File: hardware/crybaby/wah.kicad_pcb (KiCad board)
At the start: 4 copper layers, 99.1 x 87 mm, 39 parts, among them J1 Barrel_Jack_Switch, J2 In, J3 Out, J4 Conn_01x08_Pin, J5 Conn_01x08_Pin, SW2 SW_DIP_x04, SW3 SW_Push_3PDT, U1 TL072, U2 L78L05_TO92

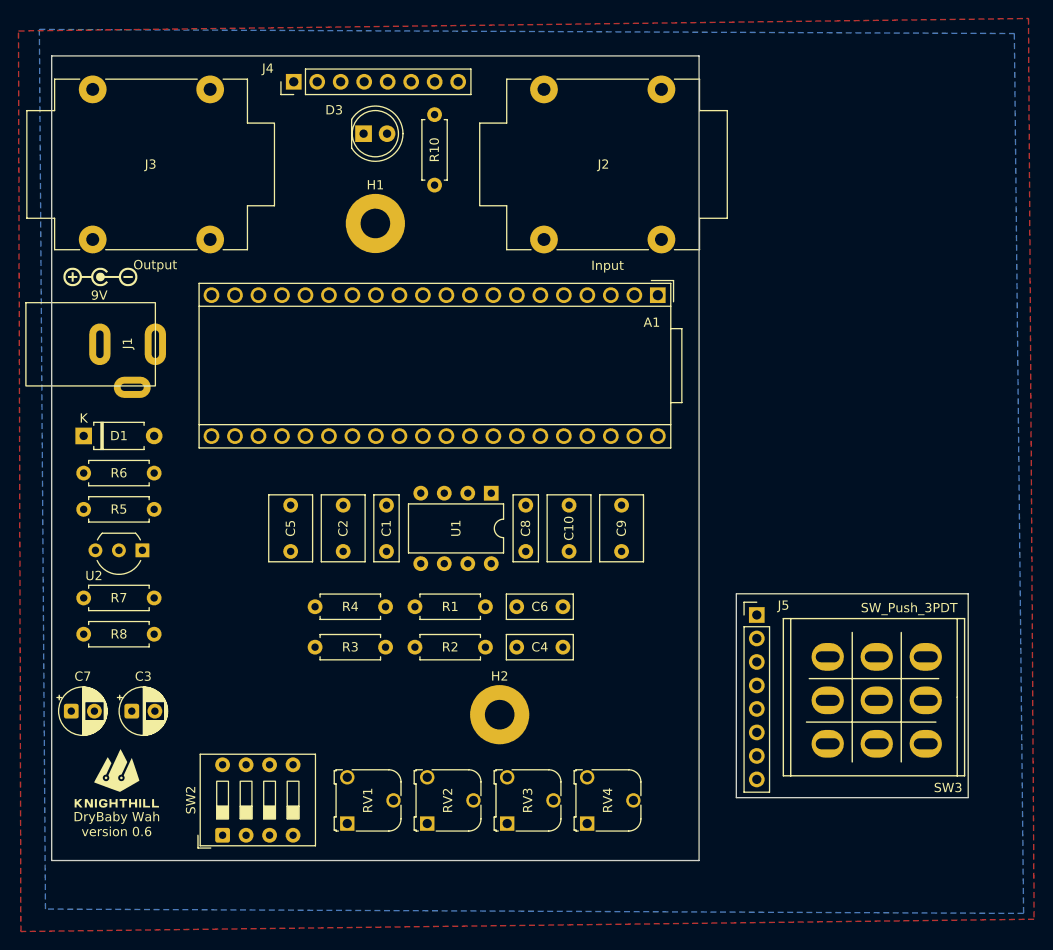
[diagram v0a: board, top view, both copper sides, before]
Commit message: major rearrangement
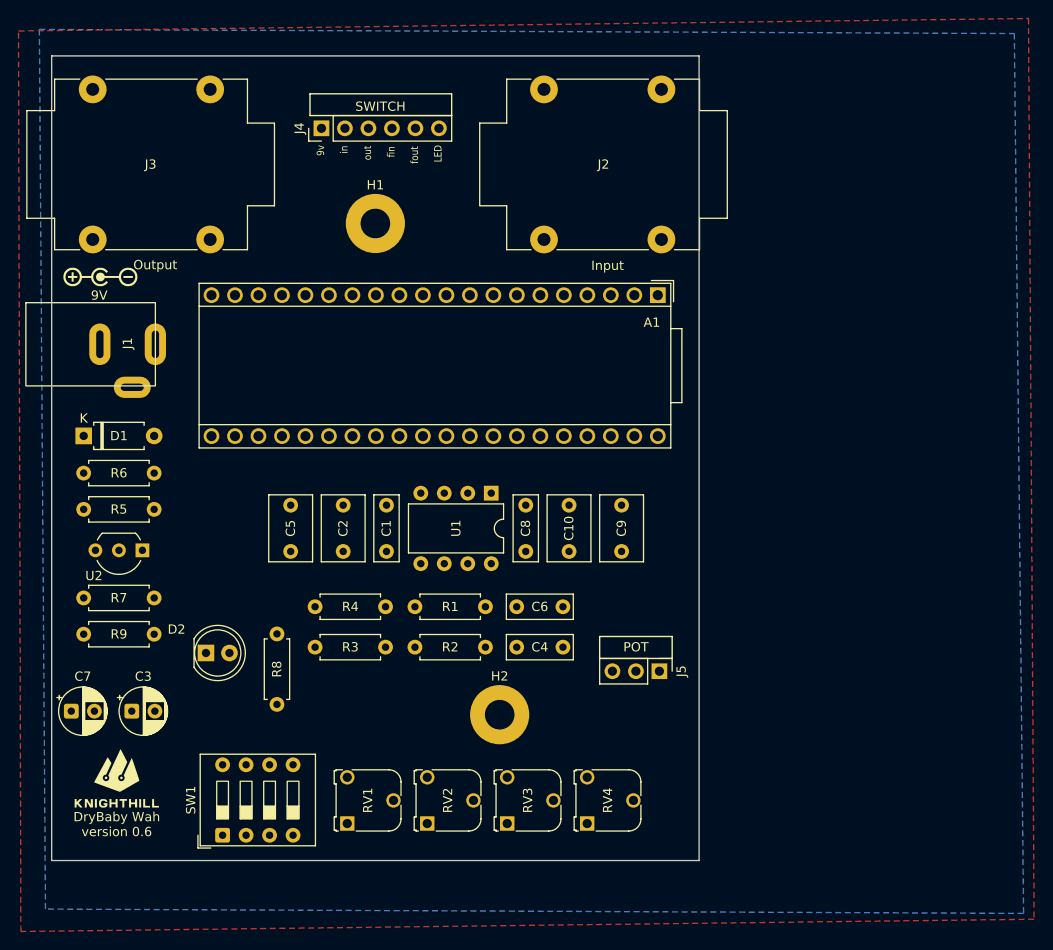
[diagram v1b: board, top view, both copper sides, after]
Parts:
- removed SW3: SW_Push_3PDT, CustomFootprints:Switches_Stomp_Switch_3PDT
- J4: value Conn_01x08_Pin -> Conn_01x06_Pin; footprint Connector_PinHeader_2.54mm:PinHeader_1x08_P2.54mm_Vertical -> Connector_PinHeader_2.54mm:PinHeader_1x06_P2.54mm_Vertical
- J5: value Conn_01x08_Pin -> Conn_01x03_Pin; footprint Connector_PinHeader_2.54mm:PinHeader_1x08_P2.54mm_Vertical -> Connector_PinHeader_2.54mm:PinHeader_1x03_P2.54mm_Vertical
- moved D2 58.7 mm to (59.2, 97.7)
- moved R8 58.7 mm to (66.8, 95.7)
- moved J5 12.2 mm to (108.2, 99.7), turned to -90 degrees
- moved J4 5.86 mm to (71.6, 41.0)
- renumbered D3 to D2, R10 to R8, R8 to R9, SW2 to SW1
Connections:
- A1 pad 26: unconnected-(A1-ADC_4-Pad26) -> /WAH_POT
- J4 pad 1: GND -> +9V
- J4 pad 2: +9V -> /J_IN
- J4 pad 3: /J_IN -> /J_OUT
- J4 pad 4: /J_OUT -> /FX_IN
- J4 pad 5: /FX_IN -> /FX_OUT
- J4 pad 6: /FX_OUT -> /LED
- J5 pad 2: Net-(J5-Pin_2) -> /WAH_POT
- J5 pad 3: Net-(J5-Pin_3) -> VDD
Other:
- board size 99.1 x 87 mm -> 70 x 87 mm
- board text added: "9v"
- board text added: "LED"
- board text added: "POT"
- board text added: "SWITCH"
- board text added: "fin"
- board text added: "fout"
- board text added: "in"
- board text added: "out"

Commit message: fix mirror
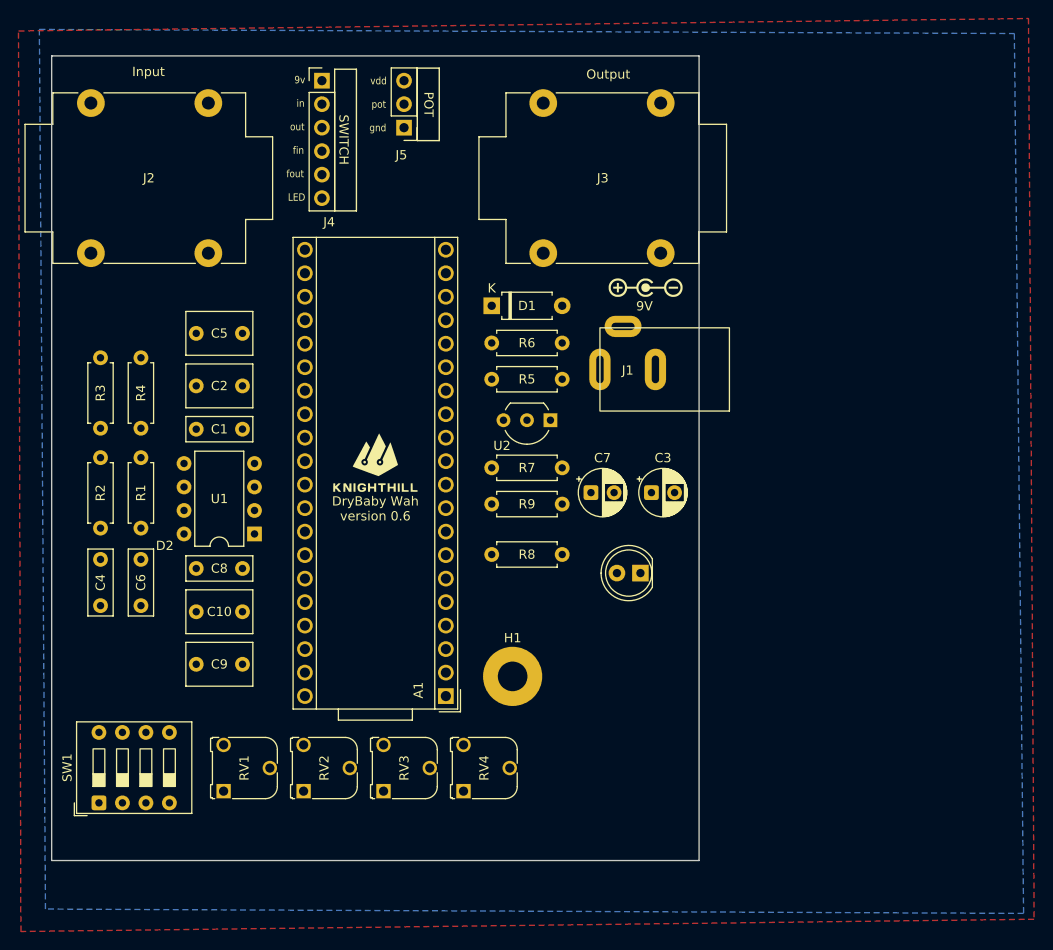
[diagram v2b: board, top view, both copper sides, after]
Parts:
- removed H2: MountingHole_Pad, MountingHole:MountingHole_3.2mm_M3_Pad
- moved J5 64.9 mm to (80.6, 40.9), turned to 180 degrees
- moved C7 61.0 mm to (100.8, 80.4)
- moved C3 61.0 mm to (107.3, 80.4)
- moved G*** 59.0 mm to (106.7, 58.2)
- moved H1 51.2 mm to (92.3, 100.2)
- moved A1 49.0 mm to (85.1, 102.4), turned to 180 degrees
- moved J1 48.1 mm to (101.8, 67.1), turned to 180 degrees
- moved D2 47.8 mm to (106.1, 89.1), turned to 180 degrees
- moved C9 47.6 mm to (58.1, 98.9), turned to 0 degrees
- moved R5 46.3 mm to (97.7, 68.1)
- moved R7 46.3 mm to (97.7, 77.7)
- moved R9 46.3 mm to (97.7, 81.6)
- moved D1 46.3 mm to (90.0, 60.2)
- moved R6 46.3 mm to (90.0, 64.2)
- moved U2 46.3 mm to (96.4, 72.5)
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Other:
- board text added: "gnd"
- board text added: "pot"
- board text added: "vdd"

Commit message: improve pcb
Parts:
- moved G*** 43.5 mm to (104.2, 112.3)
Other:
- board text added: "BadBaby Wah version 0.6"
- board text removed: "DryBaby Wah version 0.6"
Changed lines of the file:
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@@
 	(paper "A4")
 	(title_block
-		(title "Wah")
-		(date "2025-11-13")
-		(rev "0.6.1")
+		(title "BadBaby Wah")
+		(date "2025-11-16")
+		(rev "0.7")
 		(company "KnightHill Engineering")
 	)
@@
 	(footprint "LOGO"
 		(layer "F.Cu")
-		(at 77.33587 78.022106)
+		(at 104.16587 112.290059)
 		(property "Reference" "G***"
 			(at 0 0 0)
@@
 	)
 	(gr_rect
-		(start 84.376851 42.315)
-		(end 82.003148 34.475)
+		(start 82.003148 34.475)
+		(end 84.376851 42.315)
 		(stroke
 			(width 0.15)
@@
 	)
 	(gr_rect
-		(start 75.419998 49.915)
-		(end 73.069999 34.595)
+		(start 73.069999 34.595)
+		(end 75.419998 49.915)
 		(stroke
 			(width 0.15)
@@
 		)
 	)
-	(gr_text "DryBaby Wah\nversion 0.6"
-		(at 77.47 82.112106 0)
+	(gr_text "BadBaby Wah\nversion 0.6"
+		(at 104.3 116.380059 0)
 		(layer "F.SilkS")
 		(effects

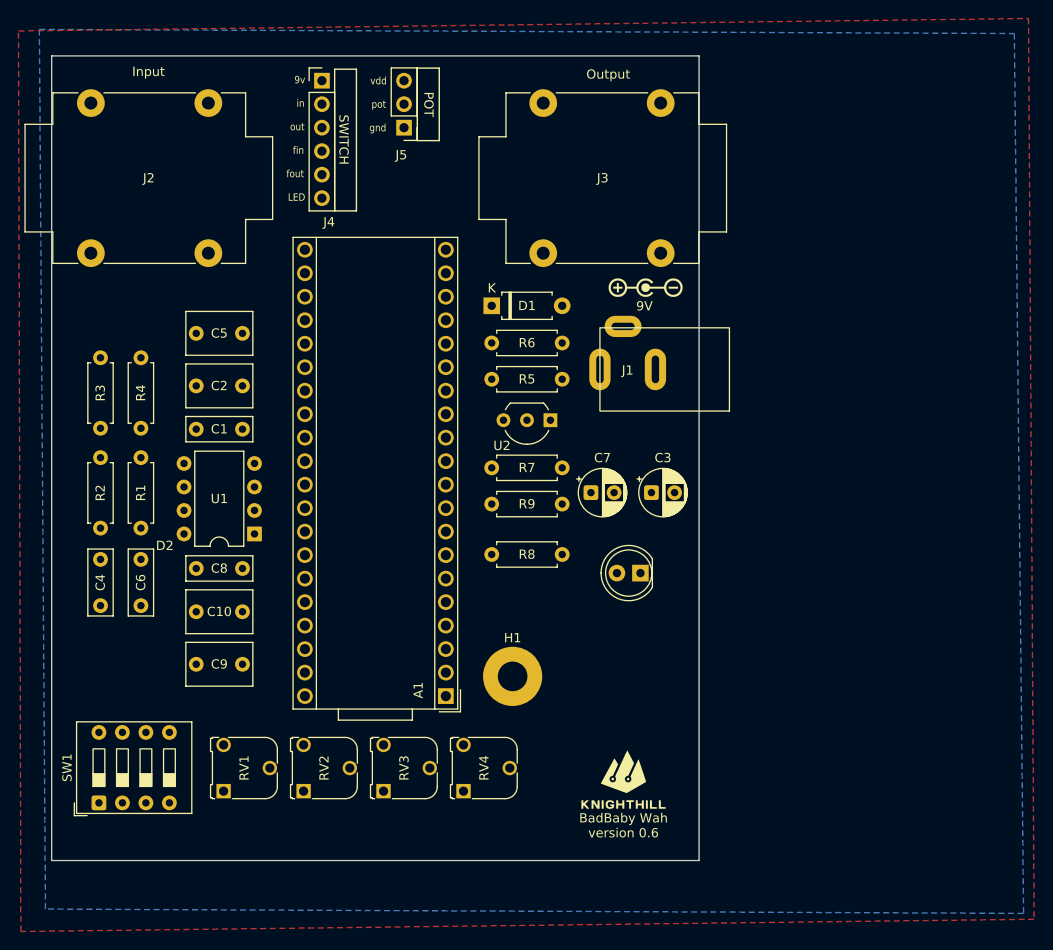
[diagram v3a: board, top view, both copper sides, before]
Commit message: add CB dimention
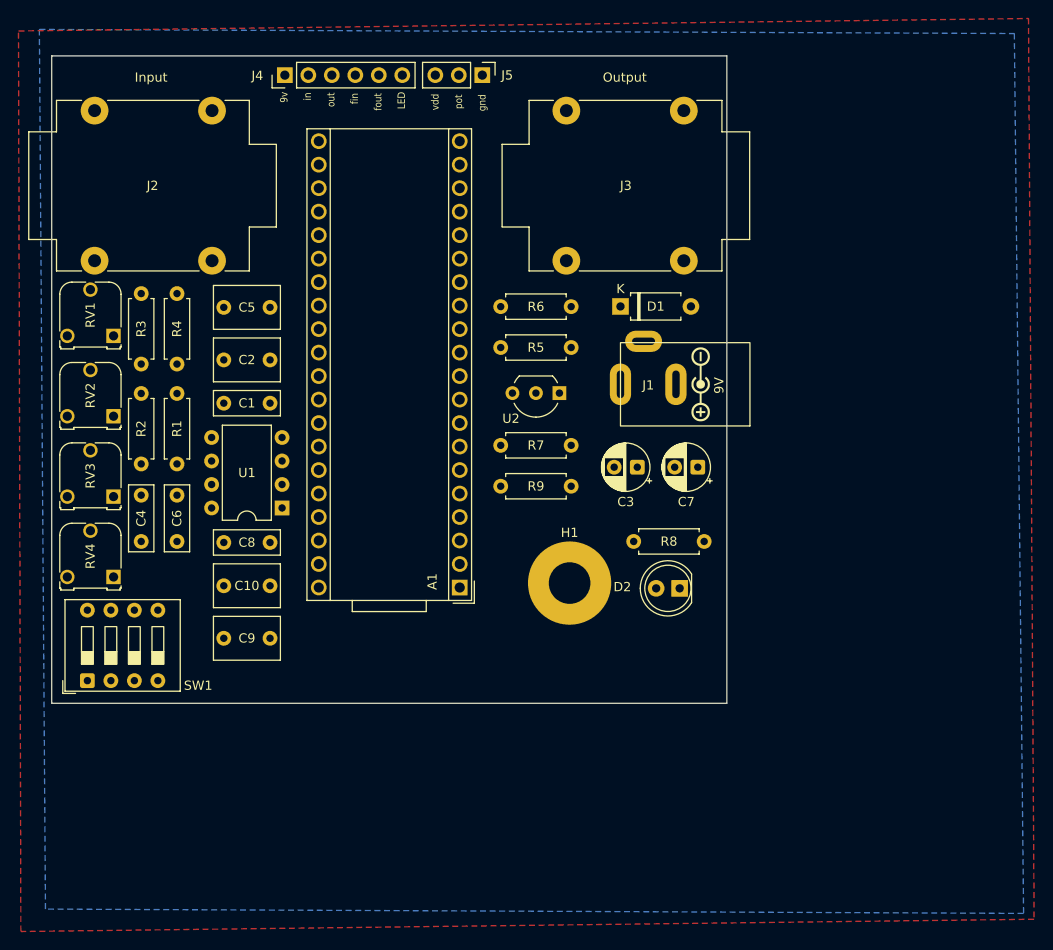
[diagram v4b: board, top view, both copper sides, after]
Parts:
- G***: moved to B.Cu
- H1: footprint MountingHole:MountingHole_3.2mm_M3_Pad -> MountingHole:MountingHole_4.5mm_Pad
- moved G*** 83.4 mm to (53.5, 46.1), turned to 180 degrees
- moved RV1 50.6 mm to (49.2, 63.4), turned to 180 degrees
- moved RV2 45.4 mm to (49.2, 72.1), turned to 180 degrees
- moved RV4 44.4 mm to (49.2, 89.5), turned to 180 degrees
- moved RV3 43.2 mm to (49.2, 80.8), turned to 180 degrees
- moved R8 15.4 mm to (105.4, 85.7)
- moved D1 13.9 mm to (104.0, 60.2)
- moved SW1 13.3 mm to (46.3, 100.7)
- moved G*** 12.0 mm to (112.6, 68.7), turned to 90 degrees
- moved C7 11.9 mm to (112.3, 77.6), turned to 180 degrees
- moved A1 11.8 mm to (86.6, 90.6)
- moved H1 11.8 mm to (98.5, 90.2)
- moved J5 10.2 mm to (89.0, 35.2), turned to -90 degrees
- moved R3 8.22 mm to (52.1, 66.5)
- moved C4 8.22 mm to (52.1, 80.7)
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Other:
- board size 70 x 87 mm -> 73 x 70 mm
- board text removed: "POT"
- board text removed: "SWITCH"

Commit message: finalze pcb
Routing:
- net /AUDIO_OUT: track 0.00 -> 83.8 mm
- net Net-(U1C-V+): track 0.00 -> 78.8 mm
- net /LED: track 0.00 -> 65.3 mm
- net /SW1: track 0.00 -> 63.9 mm
- net Net-(U1A-+): track 0.00 -> 59.9 mm
- net /SW2: track 0.00 -> 59.2 mm
- net /FX_OUT: track 0.00 -> 58.7 mm
- net /AUDIO_IN: track 0.00 -> 56.6 mm
- net /FX_IN: track 0.00 -> 54.8 mm
- net /SW3: track 0.00 -> 54.4 mm
- net /SW4: track 0.00 -> 52.1 mm
- net /POT4: track 0.00 -> 51.2 mm
- net Net-(C9-Pad2): track 0.00 -> 47.4 mm
- net /POT3: track 0.00 -> 43.8 mm
- net /POT2: track 0.00 -> 36.5 mm
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
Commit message: remove pot 4
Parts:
- removed RV4: 10k, Potentiometer_THT:Potentiometer_Runtron_RM-065_Vertical
- G***: moved to F.Cu
- RV1, RV2, RV3: footprint Potentiometer_THT:Potentiometer_Runtron_RM-065_Vertical -> Potentiometer_THT:Potentiometer_Vishay_T73YP_Vertical
- moved G*** 63.0 mm to (90.8, 96.8), turned to 0 degrees
- moved A1 49.9 mm to (71.3, 43.1), turned to 0 degrees
- moved RV1 17.8 mm to (46.8, 81.1), turned to 0 degrees
- moved RV3 16.1 mm to (46.8, 64.9), turned to 0 degrees
- moved SW1 12.6 mm to (54.9, 91.5), turned to -90 degrees
- moved RV2 2.55 mm to (46.8, 73.0), turned to 0 degrees
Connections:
- A1 pad 25: /POT4 -> unconnected-(A1-ADC_3-Pad25)
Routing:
- net /AUDIO_OUT: track 83.8 -> 17.9 mm
- net /POT4: track 51.2 -> 0.00 mm
- net /AUDIO_IN: track 56.6 -> 34.4 mm
- net /WAH_POT: track 26.1 -> 45.5 mm
- net /SW1: track 63.9 -> 47.2 mm
- net /POT1: track 30.3 -> 45.4 mm
- net /SW4: track 52.1 -> 61.9 mm
- net /POT2: track 36.5 -> 43.8 mm
- net /SW2: track 59.2 -> 52.5 mm
- net /SW3: track 54.4 -> 57.2 mm
- net /POT3: track 43.8 -> 46.1 mm
- net Net-(U1C-V+): track 78.8 -> 79.9 mm
- net Net-(U1B-+): track 19.2 -> 19.8 mm
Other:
- board text added: "BadBaby Wah version 0.8"
- board text removed: "BadBaby Wah version 0.6"

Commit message: add trimmer footprint
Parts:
- RV1, RV2, RV3: footprint Potentiometer_THT:Potentiometer_Vishay_T73YP_Vertical -> CustomFootprints:Trimmer_JBR_3362P
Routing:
- net /POT3: track 46.1 -> 48.7 mm
- net /POT2: track 43.8 -> 46.4 mm
- net /POT1: track 45.4 -> 47.1 mm

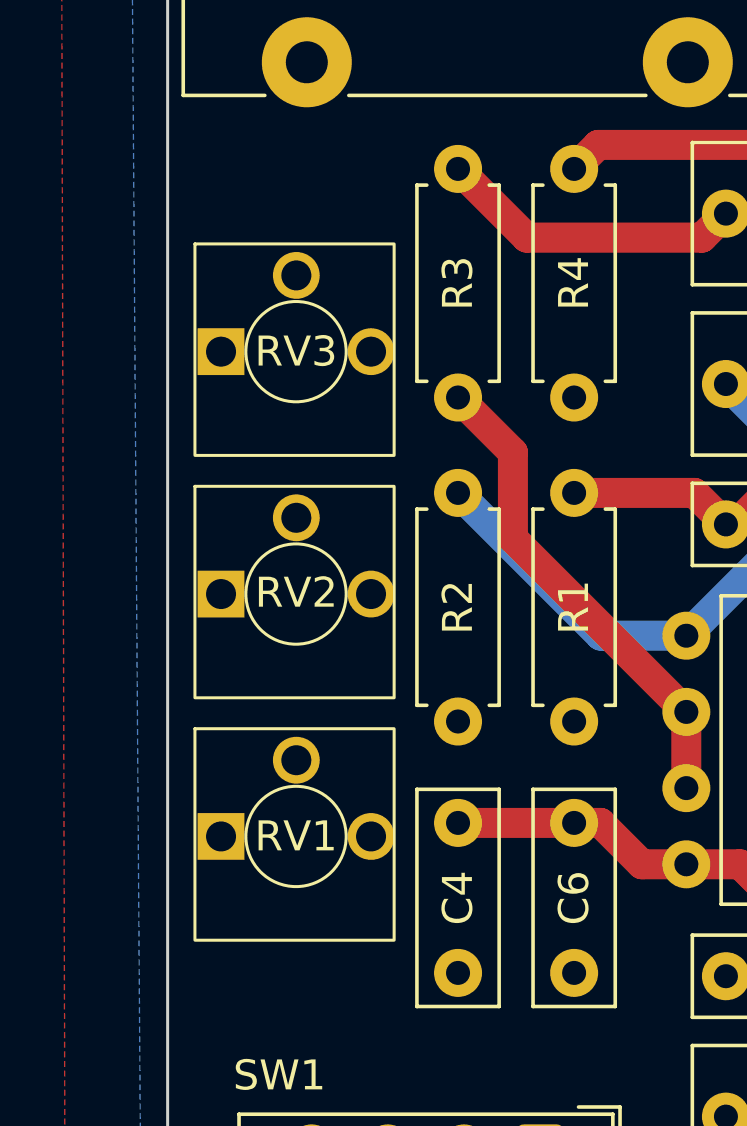
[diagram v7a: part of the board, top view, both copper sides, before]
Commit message: improve trimmer footprint
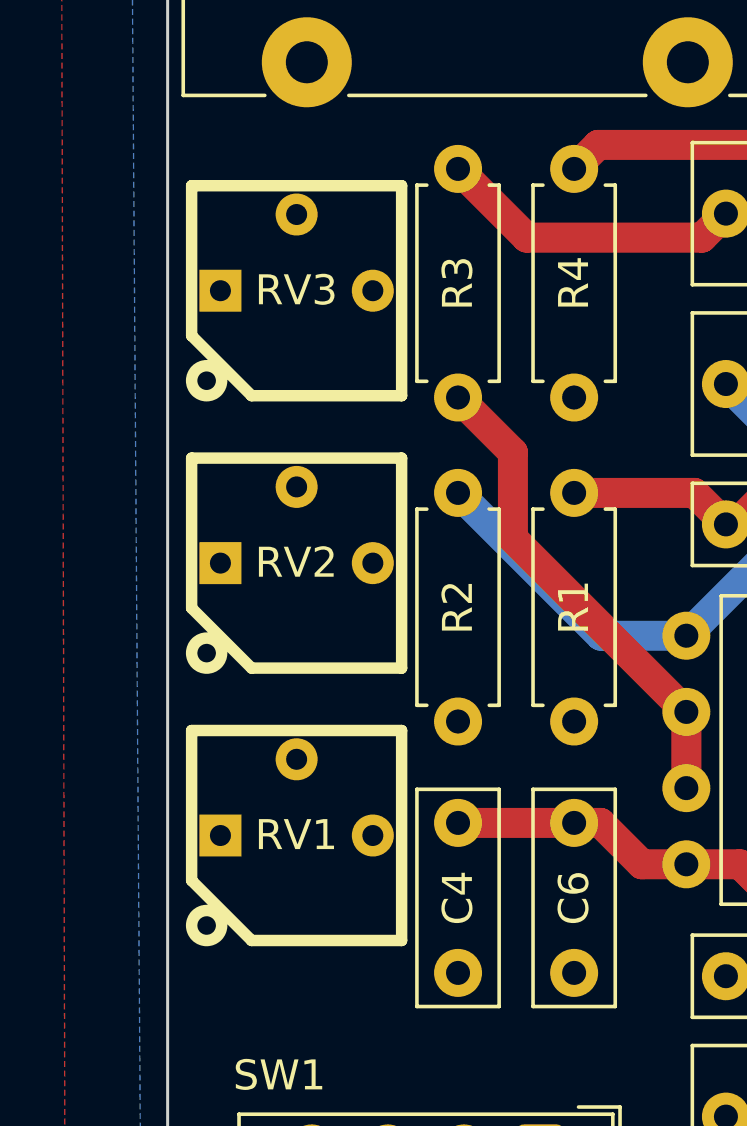
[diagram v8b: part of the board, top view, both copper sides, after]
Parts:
- RV1, RV2, RV3: footprint CustomFootprints:Trimmer_JBR_3362P -> CustomFootprints:3362P
- moved RV3 2.00 mm to (46.8, 62.9)
- moved RV2 1.00 mm to (46.8, 72.0)
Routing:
- net /POT1: track 47.1 -> 48.8 mm
- net /POT3: track 48.7 -> 49.5 mm
